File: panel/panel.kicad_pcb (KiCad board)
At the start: 2 copper layers, 20 x 128.5 mm, 10 parts

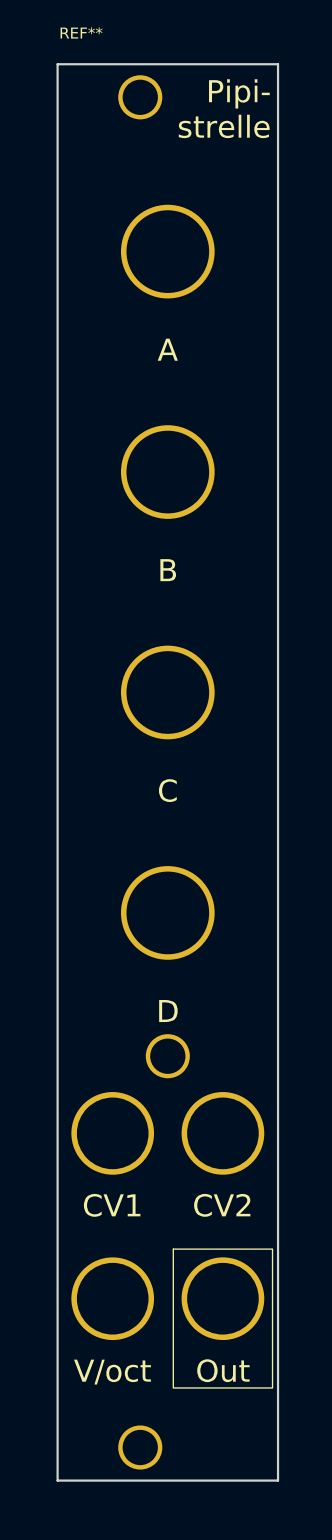
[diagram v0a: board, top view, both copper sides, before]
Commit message: Update panel footprints
Holes are now 1mm higher
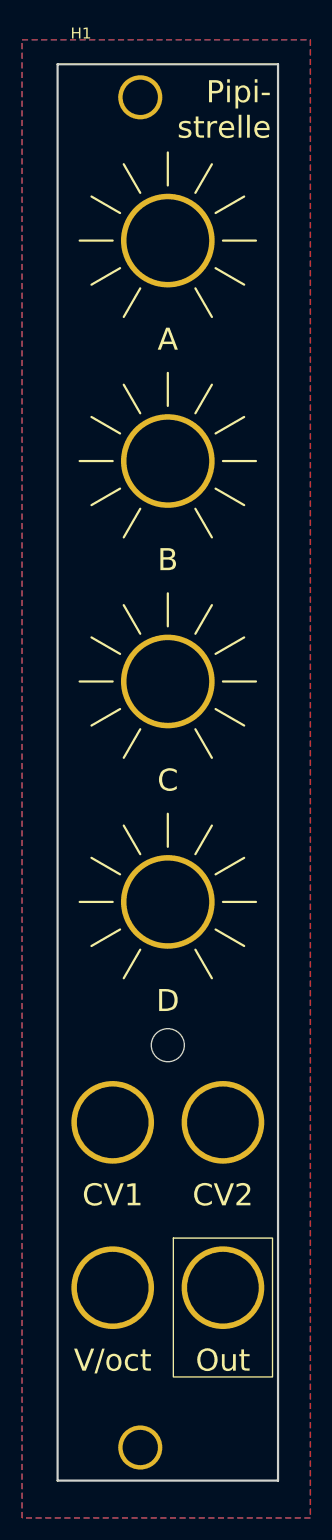
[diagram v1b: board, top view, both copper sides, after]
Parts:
- moved A 1.00 mm to (110.0, 36.0)
- moved B 1.00 mm to (110.0, 56.0)
- moved C 1.00 mm to (110.0, 76.0)
- moved CV1 1.00 mm to (105.0, 116.0)
- moved CV2 1.00 mm to (115.0, 116.0)
- moved D 1.00 mm to (110.0, 96.0)
- moved LED 1.00 mm to (110.0, 109.0)
- moved Out 1.00 mm to (115.0, 131.0)
- moved V/oct 1.00 mm to (105.0, 131.0)
- renumbered REF** to H1
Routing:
- added copper zone on B.Cu, net GND
- added copper zone on F.Cu, net GND
